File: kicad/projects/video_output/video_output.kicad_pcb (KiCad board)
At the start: 2 copper layers, 203.2 x 97.8 mm, 22 parts, among them J1 peripheral_addr_bus_connector, J2 peripheral_aux_connector, J3 peripheral_membank_connector, J4 Conn_01x16_Socket, J5 Conn_01x16_Socket, U1 628128_DIP32_SSOP32, U10 74HC157, U11 74HC157, U2 628128_DIP32_SSOP32, U3 74HC245, U4 74HC245, U5 74HC245, U6 74HC245, U7 74HC574, U8 74HC245, U9 74HC245

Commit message: Start roughing in video output.
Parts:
- added C2: 20pF, Capacitor_THT:C_Disc_D5.0mm_W2.5mm_P5.00mm, F.Cu at (-17.2, 30.1)
- added C3: 0pF, Capacitor_THT:C_Disc_D5.0mm_W2.5mm_P5.00mm, F.Cu at (-17.2, 34.1)
- added J6: Conn_01x02_Socket, Connector_PinSocket_2.54mm:PinSocket_1x02_P2.54mm_Horizontal, F.Cu at (61.0, 94.0)
- added J7: DE15_Receptacle_HighDensity, Connector_Dsub:DSUB-15_Female_Horizontal_P2.77x2.84mm_EdgePinOffset9.90mm_Housed_MountingHolesOffset11.32mm, F.Cu at (-67.9, 145.9)
- added R2: 4.7K, Resistor_THT:R_Axial_DIN0207_L6.3mm_D2.5mm_P10.16mm_Horizontal, F.Cu at (-30.5, 30.1)
- added R3: 4.7K, Resistor_THT:R_Axial_DIN0207_L6.3mm_D2.5mm_P10.16mm_Horizontal, F.Cu at (-30.5, 34.1)
- added R4: 10K, Resistor_THT:R_Axial_DIN0207_L6.3mm_D2.5mm_P10.16mm_Horizontal, F.Cu at (-30.5, 38.2)
- added R5: 10K, Resistor_THT:R_Axial_DIN0207_L6.3mm_D2.5mm_P10.16mm_Horizontal, F.Cu at (-30.5, 42.2)
- added R6: 10K, Resistor_THT:R_Axial_DIN0207_L6.3mm_D2.5mm_P10.16mm_Horizontal, F.Cu at (-30.5, 46.3)
- added R7: 10K, Resistor_THT:R_Axial_DIN0207_L6.3mm_D2.5mm_P10.16mm_Horizontal, F.Cu at (-30.5, 50.3)
- added R8: 10K, Resistor_THT:R_Axial_DIN0207_L6.3mm_D2.5mm_P10.16mm_Horizontal, F.Cu at (-30.5, 54.4)
- added R9: 10K, Resistor_THT:R_Axial_DIN0207_L6.3mm_D2.5mm_P10.16mm_Horizontal, F.Cu at (-30.5, 58.4)
- added U12: 74HC10, Package_DIP:DIP-14_W7.62mm_Socket, F.Cu at (106.7, 109.2)
- added U13: 74HC02, Package_DIP:DIP-14_W7.62mm_Socket, F.Cu at (106.7, 94.0)
- added U14: 74HC08, Package_DIP:DIP-14_W7.62mm_Socket, F.Cu at (132.1, 109.2)
- added U15: 74HC123, Package_DIP:DIP-16_W7.62mm_Socket, F.Cu at (104.1, 63.5)
- added U16: 74HC32, Package_DIP:DIP-14_W7.62mm_Socket, F.Cu at (132.1, 94.0)
- added U17: 74HC04, Package_DIP:DIP-14_W7.62mm_Socket, F.Cu at (106.7, 78.7)
- added U9: 74HC574, Package_DIP:DIP-20_W7.62mm_Socket, F.Cu at (73.7, 109.2)
- moved U6 196.8 mm to (68.6, -10.2)
- moved U3 114.3 mm to (226.1, 114.3)
- moved U9 107.2 mm to (177.8, 114.3)
- moved U2 64.3 mm to (210.8, 83.8)
- moved U5 43.4 mm to (226.1, 99.1)
- moved U1 39.4 mm to (162.6, 83.8)
- moved U10 37.5 mm to (132.1, 63.5)
- moved U4 34.1 mm to (177.8, 99.1)
- moved U11 18.0 mm to (132.1, 78.7)
- moved U8 17.0 mm to (58.4, 109.2), turned to 0 degrees
- moved U7 16.1 mm to (88.9, 109.2), turned to 0 degrees
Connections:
- J2 pad 10: /RFM -> /MEM_ACT
- J2 pad 12: /WTM -> /~{R}/W
- J4 pad 1: unconnected-(J4-Pin_1-Pad1) -> /COL_B_00
- J4 pad 10: unconnected-(J4-Pin_10-Pad10) -> /ROW_B_01
- J4 pad 11: unconnected-(J4-Pin_11-Pad11) -> /ROW_B_02
- J4 pad 12: unconnected-(J4-Pin_12-Pad12) -> /ROW_B_03
- J4 pad 13: unconnected-(J4-Pin_13-Pad13) -> /ROW_B_04
- J4 pad 14: unconnected-(J4-Pin_14-Pad14) -> /ROW_B_05
- J4 pad 15: unconnected-(J4-Pin_15-Pad15) -> /ROW_B_06
- J4 pad 2: unconnected-(J4-Pin_2-Pad2) -> /COL_B_01
- J4 pad 3: unconnected-(J4-Pin_3-Pad3) -> /COL_B_02
- J4 pad 4: unconnected-(J4-Pin_4-Pad4) -> /COL_B_03
- J4 pad 5: unconnected-(J4-Pin_5-Pad5) -> /COL_B_04
- J4 pad 6: unconnected-(J4-Pin_6-Pad6) -> /COL_B_05
- J4 pad 7: unconnected-(J4-Pin_7-Pad7) -> /COL_B_06
- J4 pad 8: unconnected-(J4-Pin_8-Pad8) -> /COL_B_07
- J4 pad 9: unconnected-(J4-Pin_9-Pad9) -> /ROW_B_00
- J5 pad 1: unconnected-(J5-Pin_1-Pad1) -> /COL_A_00
- J5 pad 10: unconnected-(J5-Pin_10-Pad10) -> /ROW_A_01
- J5 pad 11: unconnected-(J5-Pin_11-Pad11) -> /ROW_A_02
- J5 pad 12: unconnected-(J5-Pin_12-Pad12) -> /ROW_A_03
- J5 pad 13: unconnected-(J5-Pin_13-Pad13) -> /ROW_A_04
- J5 pad 14: unconnected-(J5-Pin_14-Pad14) -> /ROW_A_05
- J5 pad 15: unconnected-(J5-Pin_15-Pad15) -> /ROW_A_06
- J5 pad 2: unconnected-(J5-Pin_2-Pad2) -> /COL_A_01
- J5 pad 3: unconnected-(J5-Pin_3-Pad3) -> /COL_A_02
- J5 pad 4: unconnected-(J5-Pin_4-Pad4) -> /COL_A_03
- J5 pad 5: unconnected-(J5-Pin_5-Pad5) -> /COL_A_04
- J5 pad 6: unconnected-(J5-Pin_6-Pad6) -> /COL_A_05
- J5 pad 7: unconnected-(J5-Pin_7-Pad7) -> /COL_A_06
- J5 pad 8: unconnected-(J5-Pin_8-Pad8) -> /COL_A_07
- J5 pad 9: unconnected-(J5-Pin_9-Pad9) -> /ROW_A_00
- U1 pad 10: unconnected-(U1-A2-Pad10) -> /COL_B_02
- U1 pad 11: unconnected-(U1-A1-Pad11) -> /COL_B_01
- U1 pad 12: unconnected-(U1-A0-Pad12) -> /COL_B_00
- U1 pad 13: unconnected-(U1-Q0-Pad13) -> /PIX_R_B_00
- U1 pad 14: unconnected-(U1-Q1-Pad14) -> /PIX_R_B_01
- U1 pad 15: unconnected-(U1-Q2-Pad15) -> /PIX_G_B_00
- U1 pad 17: unconnected-(U1-Q3-Pad17) -> /PIX_G_B_01
- U1 pad 18: unconnected-(U1-Q4-Pad18) -> /PIX_B_B_00
- U1 pad 19: unconnected-(U1-Q5-Pad19) -> /PIX_B_B_01
- U1 pad 2: unconnected-(U1-A16-Pad2) -> GND
- U1 pad 20: unconnected-(U1-Q6-Pad20) -> Net-(U1-Q6)
- U1 pad 21: unconnected-(U1-Q7-Pad21) -> Net-(U1-Q7)
- U1 pad 23: unconnected-(U1-A10-Pad23) -> /ROW_B_02
- U1 pad 25: unconnected-(U1-A11-Pad25) -> /ROW_B_03
- U1 pad 26: unconnected-(U1-A9-Pad26) -> /ROW_B_01
- U1 pad 27: unconnected-(U1-A8-Pad27) -> /ROW_B_00
- U1 pad 28: unconnected-(U1-A13-Pad28) -> /ROW_B_05
- U1 pad 3: unconnected-(U1-A14-Pad3) -> /ROW_B_06
- U1 pad 31: unconnected-(U1-A15-Pad31) -> GND
- U1 pad 4: unconnected-(U1-A12-Pad4) -> /ROW_B_04
- U1 pad 5: unconnected-(U1-A7-Pad5) -> /COL_B_07
- U1 pad 6: unconnected-(U1-A6-Pad6) -> /COL_B_06
- U1 pad 7: unconnected-(U1-A5-Pad7) -> /COL_B_05
- U1 pad 8: unconnected-(U1-A4-Pad8) -> /COL_B_04
- U1 pad 9: unconnected-(U1-A3-Pad9) -> /COL_B_03
- U2 pad 10: unconnected-(U2-A2-Pad10) -> /COL_A_02
- U2 pad 11: unconnected-(U2-A1-Pad11) -> /COL_A_01
- U2 pad 12: unconnected-(U2-A0-Pad12) -> /COL_A_00
- U2 pad 13: unconnected-(U2-Q0-Pad13) -> /PIX_R_A_00
- U2 pad 14: unconnected-(U2-Q1-Pad14) -> /PIX_R_A_01
- U2 pad 15: unconnected-(U2-Q2-Pad15) -> /PIX_G_A_00
- U2 pad 17: unconnected-(U2-Q3-Pad17) -> /PIX_G_A_01
- U2 pad 18: unconnected-(U2-Q4-Pad18) -> /PIX_B_A_00
- U2 pad 19: unconnected-(U2-Q5-Pad19) -> /PIX_B_A_01
- U2 pad 2: unconnected-(U2-A16-Pad2) -> GND
- U2 pad 20: unconnected-(U2-Q6-Pad20) -> Net-(U2-Q6)
- U2 pad 21: unconnected-(U2-Q7-Pad21) -> Net-(U2-Q7)
- U2 pad 23: unconnected-(U2-A10-Pad23) -> /ROW_A_02
- U2 pad 25: unconnected-(U2-A11-Pad25) -> /ROW_A_03
- U2 pad 26: unconnected-(U2-A9-Pad26) -> /ROW_A_01
- U2 pad 27: unconnected-(U2-A8-Pad27) -> /ROW_A_00
- U2 pad 28: unconnected-(U2-A13-Pad28) -> /ROW_A_05
- U2 pad 3: unconnected-(U2-A14-Pad3) -> /ROW_A_06
- U2 pad 31: unconnected-(U2-A15-Pad31) -> GND
- U2 pad 4: unconnected-(U2-A12-Pad4) -> /ROW_A_04
- U2 pad 5: unconnected-(U2-A7-Pad5) -> /COL_A_07
- U2 pad 6: unconnected-(U2-A6-Pad6) -> /COL_A_06
- U2 pad 7: unconnected-(U2-A5-Pad7) -> /COL_A_05
- U2 pad 8: unconnected-(U2-A4-Pad8) -> /COL_A_04
- U2 pad 9: unconnected-(U2-A3-Pad9) -> /COL_A_03

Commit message: Bit of work on video output schematic.
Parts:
- added C4: C, Capacitor_THT:C_Disc_D5.0mm_W2.5mm_P5.00mm, F.Cu at (-35.6, 76.3)
- added C5: C, Capacitor_THT:C_Disc_D5.0mm_W2.5mm_P5.00mm, F.Cu at (-35.6, 80.3)
- added C6: C, Capacitor_THT:C_Disc_D5.0mm_W2.5mm_P5.00mm, F.Cu at (-35.6, 84.4)
- added C7: C, Capacitor_THT:C_Disc_D5.0mm_W2.5mm_P5.00mm, F.Cu at (-35.6, 88.4)
- added C8: C, Capacitor_THT:C_Disc_D5.0mm_W2.5mm_P5.00mm, F.Cu at (-35.6, 92.5)
- added C9: C, Capacitor_THT:C_Disc_D5.0mm_W2.5mm_P5.00mm, F.Cu at (-35.6, 96.5)
- added RN1: 10K, Resistor_THT:R_Array_SIP5, F.Cu at (248.9, 104.1)
- added RN2: 10K, Resistor_THT:R_Array_SIP5, F.Cu at (205.7, 104.1)
- added RN3: 10K, Resistor_THT:R_Array_SIP5, F.Cu at (248.9, 121.9)
- added RN4: 10K, Resistor_THT:R_Array_SIP5, F.Cu at (205.7, 121.9)
- moved U6 167.8 mm to (175.3, 119.4)
- moved U9 152.6 mm to (25.4, 121.9)
- moved U5 21.7 mm to (218.4, 119.4)
- moved U3 14.8 mm to (218.4, 101.6)
- moved U4 3.59 mm to (175.3, 101.6)
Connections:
- U1 pad 13: /PIX_R_B_00 -> /PIX_B_R_00
- U1 pad 14: /PIX_R_B_01 -> /PIX_B_R_01
- U1 pad 15: /PIX_G_B_00 -> /PIX_B_G_00
- U1 pad 16: unconnected-(U1-GND-Pad16) -> GND
- U1 pad 17: /PIX_G_B_01 -> /PIX_B_G_01
- U1 pad 22: unconnected-(U1-~{CS1}-Pad22) -> GND
- U1 pad 24: unconnected-(U1-~{OE}-Pad24) -> GND
- U1 pad 29: unconnected-(U1-~{WE}-Pad29) -> /B_RAM_~{WE}
- U1 pad 30: unconnected-(U1-CS2-Pad30) -> VCC
- U1 pad 32: unconnected-(U1-VCC-Pad32) -> VCC
- U10 pad 10: unconnected-(U10-3B-Pad10) -> VCC
- U10 pad 11: unconnected-(U10-3A-Pad11) -> /RAM_~{WE}
- U10 pad 15: unconnected-(U10-~{G}-Pad15) -> GND
- U10 pad 2: unconnected-(U10-1A-Pad2) -> /DATA_BUF_~{OE}
- U10 pad 3: unconnected-(U10-1B-Pad3) -> VCC
- U10 pad 4: unconnected-(U10-1Y-Pad4) -> /B_DATA_BUF_~{OE}
- U10 pad 5: unconnected-(U10-2A-Pad5) -> /DATA_BUF_DIR
- U10 pad 6: unconnected-(U10-2B-Pad6) -> GND
- U10 pad 7: unconnected-(U10-2Y-Pad7) -> /B_DATA_BUF_DIR
- U10 pad 9: unconnected-(U10-3Y-Pad9) -> /B_RAM_~{WE}
- U11 pad 10: unconnected-(U11-3B-Pad10) -> VCC
- U11 pad 11: unconnected-(U11-3A-Pad11) -> /RAM_~{WE}
- U11 pad 15: unconnected-(U11-~{G}-Pad15) -> GND
- U11 pad 2: unconnected-(U11-1A-Pad2) -> /DATA_BUF_~{OE}
- U11 pad 3: unconnected-(U11-1B-Pad3) -> VCC
- U11 pad 4: unconnected-(U11-1Y-Pad4) -> /A_DATA_BUF_~{OE}
- U11 pad 5: unconnected-(U11-2A-Pad5) -> /DATA_BUF_DIR
- U11 pad 6: unconnected-(U11-2B-Pad6) -> GND
- U11 pad 7: unconnected-(U11-2Y-Pad7) -> /A_DATA_BUF_DIR
- U11 pad 9: unconnected-(U11-3Y-Pad9) -> /A_RAM_~{WE}
- U14 pad 11: /DATA_BUF_DIR -> Net-(U14-Pad11)
- U16 pad 1: /DATA_BUF_DIR -> Net-(U14-Pad11)
- U2 pad 13: /PIX_R_A_00 -> /PIX_A_R_00
- U2 pad 14: /PIX_R_A_01 -> /PIX_A_R_01
- U2 pad 15: /PIX_G_A_00 -> /PIX_A_G_00
- U2 pad 16: unconnected-(U2-GND-Pad16) -> GND
- U2 pad 17: /PIX_G_A_01 -> /PIX_A_G_01
- U2 pad 18: /PIX_B_A_00 -> /PIX_A_B_00
- U2 pad 19: /PIX_B_A_01 -> /PIX_A_B_01
- U2 pad 22: unconnected-(U2-~{CS1}-Pad22) -> GND
- U2 pad 24: unconnected-(U2-~{OE}-Pad24) -> GND
- U2 pad 29: unconnected-(U2-~{WE}-Pad29) -> /A_RAM_~{WE}
- U2 pad 30: unconnected-(U2-CS2-Pad30) -> VCC
- U2 pad 32: unconnected-(U2-VCC-Pad32) -> VCC
- U3 pad 10: unconnected-(U3-GND-Pad10) -> GND
- U3 pad 11: unconnected-(U3-B8-Pad11) -> Net-(RN1-R3)
- U3 pad 12: unconnected-(U3-B7-Pad12) -> Net-(RN1-R4)
- U3 pad 13: unconnected-(U3-B6-Pad13) -> /PIX_A_R_00
- U3 pad 14: unconnected-(U3-B5-Pad14) -> /PIX_A_R_01
- U3 pad 15: unconnected-(U3-B4-Pad15) -> /PIX_A_G_00
- U3 pad 16: unconnected-(U3-B3-Pad16) -> /PIX_A_G_01
- U3 pad 17: unconnected-(U3-B2-Pad17) -> /PIX_A_B_00
- U3 pad 18: unconnected-(U3-B1-Pad18) -> /PIX_A_B_01
- U3 pad 2: unconnected-(U3-A1-Pad2) -> /PIX_B_01
- U3 pad 20: unconnected-(U3-VCC-Pad20) -> VCC
- U3 pad 3: unconnected-(U3-A2-Pad3) -> /PIX_B_00
- U3 pad 4: unconnected-(U3-A3-Pad4) -> /PIX_G_01
- U3 pad 5: unconnected-(U3-A3-Pad5) -> /PIX_G_00
- U3 pad 6: unconnected-(U3-A5-Pad6) -> /PIX_R_01
- U3 pad 7: unconnected-(U3-A6-Pad7) -> /PIX_R_00
- U3 pad 8: unconnected-(U3-A7-Pad8) -> Net-(RN1-R1)
- U3 pad 9: unconnected-(U3-A8-Pad9) -> Net-(RN1-R2)
- U4 pad 10: unconnected-(U4-GND-Pad10) -> GND
- U4 pad 11: unconnected-(U4-B8-Pad11) -> Net-(RN2-R3)
- U4 pad 12: unconnected-(U4-B7-Pad12) -> Net-(RN2-R4)
- U4 pad 13: unconnected-(U4-B6-Pad13) -> /PIX_B_R_00
- U4 pad 14: unconnected-(U4-B5-Pad14) -> /PIX_B_R_01
- U4 pad 15: unconnected-(U4-B4-Pad15) -> /PIX_B_G_00
- U4 pad 16: unconnected-(U4-B3-Pad16) -> /PIX_B_G_01
- U4 pad 17: unconnected-(U4-B2-Pad17) -> /PIX_B_B_00
- U4 pad 18: unconnected-(U4-B1-Pad18) -> /PIX_B_B_01
- U4 pad 2: unconnected-(U4-A1-Pad2) -> /PIX_B_01
- U4 pad 20: unconnected-(U4-VCC-Pad20) -> VCC
- U4 pad 3: unconnected-(U4-A2-Pad3) -> /PIX_B_00
- U4 pad 4: unconnected-(U4-A3-Pad4) -> /PIX_G_01
- U4 pad 5: unconnected-(U4-A3-Pad5) -> /PIX_G_00
- U4 pad 6: unconnected-(U4-A5-Pad6) -> /PIX_R_01
- U4 pad 7: unconnected-(U4-A6-Pad7) -> /PIX_R_00
- U4 pad 8: unconnected-(U4-A7-Pad8) -> Net-(RN2-R1)
- U4 pad 9: unconnected-(U4-A8-Pad9) -> Net-(RN2-R2)
- U5 pad 10: unconnected-(U5-GND-Pad10) -> GND
- U5 pad 11: unconnected-(U5-B8-Pad11) -> Net-(RN3-R3)
- U5 pad 12: unconnected-(U5-B7-Pad12) -> Net-(RN3-R4)
- U5 pad 13: unconnected-(U5-B6-Pad13) -> /PIX_A_R_00
- U5 pad 14: unconnected-(U5-B5-Pad14) -> /PIX_A_R_01
- U5 pad 15: unconnected-(U5-B4-Pad15) -> /PIX_A_G_00
- U5 pad 16: unconnected-(U5-B3-Pad16) -> /PIX_A_G_01
- U5 pad 17: unconnected-(U5-B2-Pad17) -> /PIX_A_B_00
- U5 pad 18: unconnected-(U5-B1-Pad18) -> /PIX_A_B_01
- U5 pad 2: unconnected-(U5-A1-Pad2) -> /DATA_BUS_05
- U5 pad 20: unconnected-(U5-VCC-Pad20) -> VCC
- U5 pad 3: unconnected-(U5-A2-Pad3) -> /DATA_BUS_04
- U5 pad 4: unconnected-(U5-A3-Pad4) -> /DATA_BUS_03
- U5 pad 5: unconnected-(U5-A3-Pad5) -> /DATA_BUS_02
- U5 pad 6: unconnected-(U5-A5-Pad6) -> /DATA_BUS_01
- U5 pad 7: unconnected-(U5-A6-Pad7) -> /DATA_BUS_00
- U5 pad 8: unconnected-(U5-A7-Pad8) -> Net-(RN3-R1)
- U5 pad 9: unconnected-(U5-A8-Pad9) -> Net-(RN3-R2)
- U6 pad 10: unconnected-(U6-GND-Pad10) -> GND
- U6 pad 11: unconnected-(U6-B8-Pad11) -> Net-(RN4-R3)
- U6 pad 12: unconnected-(U6-B7-Pad12) -> Net-(RN4-R4)
- U6 pad 13: unconnected-(U6-B6-Pad13) -> /PIX_B_R_00
- U6 pad 14: unconnected-(U6-B5-Pad14) -> /PIX_B_R_01
- U6 pad 15: unconnected-(U6-B4-Pad15) -> /PIX_B_G_00
- U6 pad 16: unconnected-(U6-B3-Pad16) -> /PIX_B_G_01
- U6 pad 17: unconnected-(U6-B2-Pad17) -> /PIX_B_B_00
- U6 pad 18: unconnected-(U6-B1-Pad18) -> /PIX_B_B_01
- U6 pad 2: unconnected-(U6-A1-Pad2) -> /DATA_BUS_05
- U6 pad 20: unconnected-(U6-VCC-Pad20) -> VCC
- U6 pad 3: unconnected-(U6-A2-Pad3) -> /DATA_BUS_04
- U6 pad 4: unconnected-(U6-A3-Pad4) -> /DATA_BUS_03
- U6 pad 5: unconnected-(U6-A3-Pad5) -> /DATA_BUS_02
- U6 pad 6: unconnected-(U6-A5-Pad6) -> /DATA_BUS_01
- U6 pad 7: unconnected-(U6-A6-Pad7) -> /DATA_BUS_00
- U6 pad 8: unconnected-(U6-A7-Pad8) -> Net-(RN4-R1)
- U6 pad 9: unconnected-(U6-A8-Pad9) -> Net-(RN4-R2)
- U7 pad 1: unconnected-(U7-OE-Pad1) -> GND
- U7 pad 18: unconnected-(U7-Q1-Pad18) -> /VSYNC_CLOCKED
- U7 pad 19: unconnected-(U7-Q0-Pad19) -> /HSYNC_CLOCKED
- U7 pad 2: unconnected-(U7-D0-Pad2) -> /HSYNC
- U7 pad 3: unconnected-(U7-D1-Pad3) -> /VSYNC
- U7 pad 4: unconnected-(U7-D2-Pad4) -> GND
- U7 pad 5: unconnected-(U7-D3-Pad5) -> GND
- U7 pad 6: unconnected-(U7-D4-Pad6) -> GND
- U7 pad 7: unconnected-(U7-D5-Pad7) -> GND
- U7 pad 8: unconnected-(U7-D6-Pad8) -> GND
- U7 pad 9: unconnected-(U7-D7-Pad9) -> GND
- U8 pad 2: unconnected-(U8-A1-Pad2) -> /PIX_R_00_CLOCKED
- U8 pad 3: unconnected-(U8-A2-Pad3) -> /PIX_R_01_CLOCKED
- U8 pad 4: unconnected-(U8-A3-Pad4) -> /PIX_G_00_CLOCKED
- U8 pad 5: unconnected-(U8-A3-Pad5) -> /PIX_G_01_CLOCKED
- U8 pad 6: unconnected-(U8-A5-Pad6) -> /PIX_B_00_CLOCKED
- U8 pad 7: unconnected-(U8-A6-Pad7) -> /PIX_B_01_CLOCKED
- U8 pad 8: unconnected-(U8-A7-Pad8) -> /HSYNC_CLOCKED
- U8 pad 9: unconnected-(U8-A8-Pad9) -> /VSYNC_CLOCKED
- U9 pad 14: unconnected-(U9-Q5-Pad14) -> /PIX_B_01_CLOCKED
- U9 pad 15: unconnected-(U9-Q4-Pad15) -> /PIX_B_00_CLOCKED
- U9 pad 16: unconnected-(U9-Q3-Pad16) -> /PIX_G_01_CLOCKED
- U9 pad 17: unconnected-(U9-Q2-Pad17) -> /PIX_G_00_CLOCKED
- U9 pad 18: unconnected-(U9-Q1-Pad18) -> /PIX_R_01_CLOCKED
- U9 pad 19: unconnected-(U9-Q0-Pad19) -> /PIX_R_00_CLOCKED
- U9 pad 2: unconnected-(U9-D0-Pad2) -> /PIX_R_00
- U9 pad 3: unconnected-(U9-D1-Pad3) -> /PIX_R_01
- U9 pad 4: unconnected-(U9-D2-Pad4) -> /PIX_G_00
- U9 pad 5: unconnected-(U9-D3-Pad5) -> /PIX_G_01
- U9 pad 6: unconnected-(U9-D4-Pad6) -> /PIX_B_00
- U9 pad 7: unconnected-(U9-D5-Pad7) -> /PIX_B_01
- U9 pad 8: unconnected-(U9-D6-Pad8) -> GND
- U9 pad 9: unconnected-(U9-D7-Pad9) -> GND

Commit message: Add music planning and some extra work planning video card layouts.
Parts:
- removed the U9 at (25.4, 121.9)
- added C10: C, Capacitor_THT:C_Disc_D5.0mm_W2.5mm_P5.00mm, F.Cu at (-45.6, 42.2)
- added C11: C, Capacitor_THT:C_Disc_D5.0mm_W2.5mm_P5.00mm, F.Cu at (-45.6, 46.3)
- added C12: C, Capacitor_THT:C_Disc_D5.0mm_W2.5mm_P5.00mm, F.Cu at (-45.6, 50.3)
- added C13: C, Capacitor_THT:C_Disc_D5.0mm_W2.5mm_P5.00mm, F.Cu at (-45.6, 54.4)
- added C14: C, Capacitor_THT:C_Disc_D5.0mm_W2.5mm_P5.00mm, F.Cu at (-45.6, 58.4)
- moved U14 39.7 mm to (106.7, 78.7)
- moved U17 39.7 mm to (132.1, 109.2)
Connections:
- U10 pad 16: unconnected-(U10-VCC-Pad16) -> VCC
- U10 pad 8: unconnected-(U10-GND-Pad8) -> GND
- U11 pad 16: unconnected-(U11-VCC-Pad16) -> VCC
- U11 pad 8: unconnected-(U11-GND-Pad8) -> GND
- U7 pad 10: unconnected-(U7-GND-Pad10) -> GND
- U7 pad 11: unconnected-(U7-Cp-Pad11) -> /PIXEL_CLK
- U7 pad 17: unconnected-(U7-Q2-Pad17) -> /ANYBLANK_CLOCKED
- U7 pad 20: unconnected-(U7-VCC-Pad20) -> VCC
- U7 pad 4: GND -> /ANYBLANK
- U8 pad 10: unconnected-(U8-GND-Pad10) -> GND
- U8 pad 20: unconnected-(U8-VCC-Pad20) -> VCC
- U9 pad 10: unconnected-(U9-GND-Pad10) -> GND
- U9 pad 11: unconnected-(U9-Cp-Pad11) -> /PIXEL_CLK
- U9 pad 20: unconnected-(U9-VCC-Pad20) -> VCC

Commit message: Bit more tweaking and fleshing out of video circuits.
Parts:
- added R10: 1.5K, Resistor_THT:R_Axial_DIN0207_L6.3mm_D2.5mm_P10.16mm_Horizontal, F.Cu at (68.7, 104.1)
- added R11: 680, Resistor_THT:R_Axial_DIN0207_L6.3mm_D2.5mm_P10.16mm_Horizontal, F.Cu at (72.7, 104.1)
- added R12: 1.5K, Resistor_THT:R_Axial_DIN0207_L6.3mm_D2.5mm_P10.16mm_Horizontal, F.Cu at (76.8, 104.1)
- added R13: 680, Resistor_THT:R_Axial_DIN0207_L6.3mm_D2.5mm_P10.16mm_Horizontal, F.Cu at (80.8, 104.1)
- added R14: 1.5K, Resistor_THT:R_Axial_DIN0207_L6.3mm_D2.5mm_P10.16mm_Horizontal, F.Cu at (84.8, 104.1)
- added R15: 680, Resistor_THT:R_Axial_DIN0207_L6.3mm_D2.5mm_P10.16mm_Horizontal, F.Cu at (88.9, 104.1)
- added RN5: 10K, Resistor_THT:R_Array_SIP9, F.Cu at (53.3, 132.1)
- moved R5 273.3 mm to (238.8, 88.9)
- moved R6 260.1 mm to (226.1, 88.9)
- moved R7 224.3 mm to (190.5, 88.9)
- moved R8 211.1 mm to (177.8, 88.9)
- moved R4 160.1 mm to (129.5, 43.2)
- moved R2 148.1 mm to (116.8, 45.7), turned to 180 degrees
- moved R3 137.3 mm to (106.7, 40.6)
- moved C3 123.9 mm to (106.7, 35.6)
- moved C2 123.9 mm to (106.7, 30.1)
- moved R9 96.4 mm to (61.0, 88.9)
- moved U16 15.2 mm to (132.1, 109.2)
- moved U17 15.2 mm to (132.1, 94.0)
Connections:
- U10 pad 1: unconnected-(U10-~{A}/B-Pad1) -> /~{BANK_SEL}
- U10 pad 13: unconnected-(U10-4B-Pad13) -> GND
- U10 pad 14: unconnected-(U10-4A-Pad14) -> GND
- U11 pad 1: unconnected-(U11-~{A}/B-Pad1) -> /BANK_SEL
- U11 pad 13: unconnected-(U11-4B-Pad13) -> GND
- U11 pad 14: unconnected-(U11-4A-Pad14) -> GND
- U16 pad 11: unconnected-(U16-Pad11) -> /ANYBLANK
- U16 pad 12: unconnected-(U16-Pad12) -> /HBLANK_CLOCKED
- U16 pad 13: unconnected-(U16-Pad13) -> /VBLANK_CLOCKED
- U17 pad 5: unconnected-(U17-Pad5) -> /BANK_SEL
- U17 pad 6: unconnected-(U17-Pad6) -> /~{BANK_SEL}
- U3 pad 1: unconnected-(U3-DIR-Pad1) -> GND
- U3 pad 19: unconnected-(U3-~{OE}-Pad19) -> /~{BANK_SEL}
- U4 pad 1: unconnected-(U4-DIR-Pad1) -> GND
- U4 pad 19: unconnected-(U4-~{OE}-Pad19) -> /BANK_SEL
- U5 pad 1: unconnected-(U5-DIR-Pad1) -> /A_DATA_BUF_DIR
- U5 pad 19: unconnected-(U5-~{OE}-Pad19) -> /A_DATA_BUF_~{OE}
- U6 pad 1: unconnected-(U6-DIR-Pad1) -> /B_DATA_BUF_DIR
- U6 pad 19: unconnected-(U6-~{OE}-Pad19) -> /B_DATA_BUF_~{OE}
- U7 pad 16: unconnected-(U7-Q3-Pad16) -> /VBLANK_CLOCKED
- U7 pad 17: /ANYBLANK_CLOCKED -> /HBLANK_CLOCKED
- U7 pad 4: /ANYBLANK -> /HBLANK
- U7 pad 5: GND -> /VBLANK
- U8 pad 1: unconnected-(U8-DIR-Pad1) -> VCC
- U8 pad 11: unconnected-(U8-B8-Pad11) -> /VSYNC_OUT
- U8 pad 12: unconnected-(U8-B7-Pad12) -> /HSYNC_OUT
- U8 pad 13: unconnected-(U8-B6-Pad13) -> /PIX_B_01_OUT
- U8 pad 14: unconnected-(U8-B5-Pad14) -> /PIX_B_00_OUT
- U8 pad 15: unconnected-(U8-B4-Pad15) -> /PIX_G_01_OUT
- U8 pad 16: unconnected-(U8-B3-Pad16) -> /PIX_G_00_OUT
- U8 pad 17: unconnected-(U8-B2-Pad17) -> /PIX_R_01_OUT
- U8 pad 18: unconnected-(U8-B1-Pad18) -> /PIX_R_00_OUT
- U8 pad 19: unconnected-(U8-~{OE}-Pad19) -> GND
- U9 pad 1: unconnected-(U9-OE-Pad1) -> /ANYBLANK

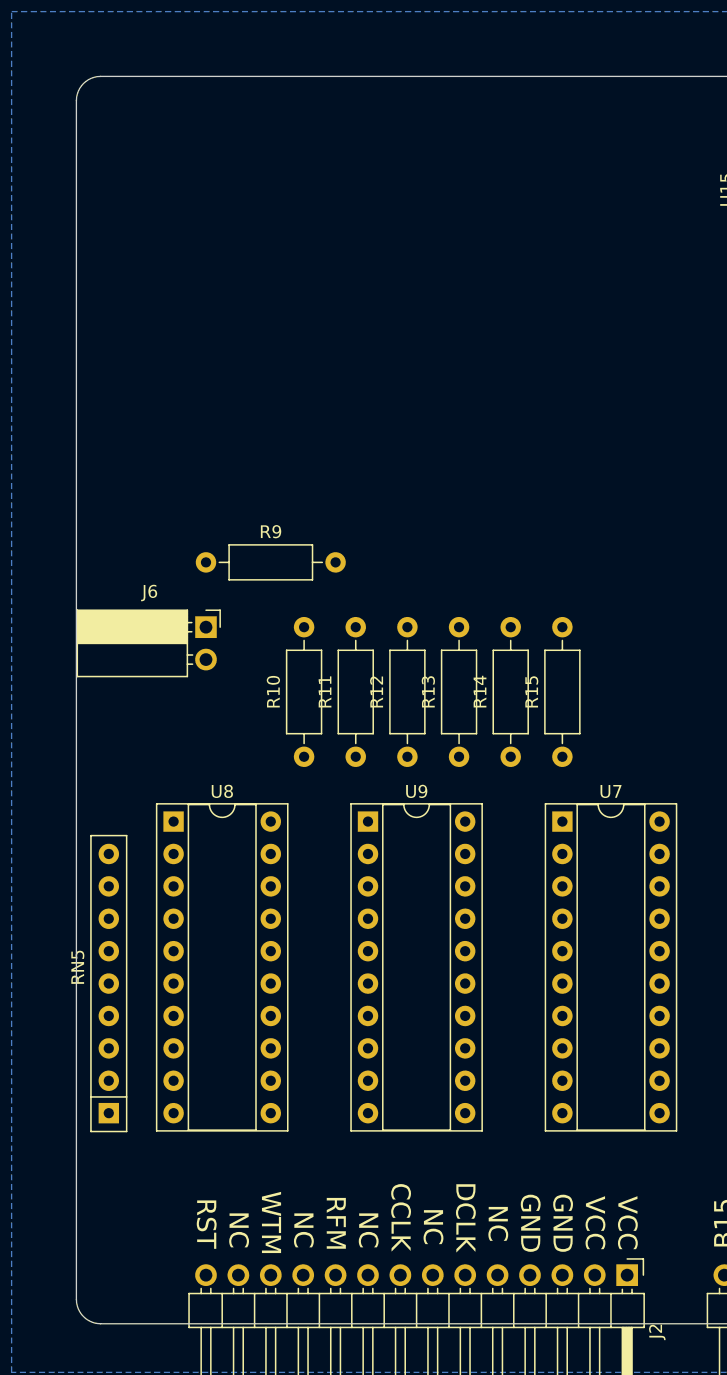
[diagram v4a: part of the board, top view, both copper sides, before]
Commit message: Adding video aux and some bits and bieces on video boards.
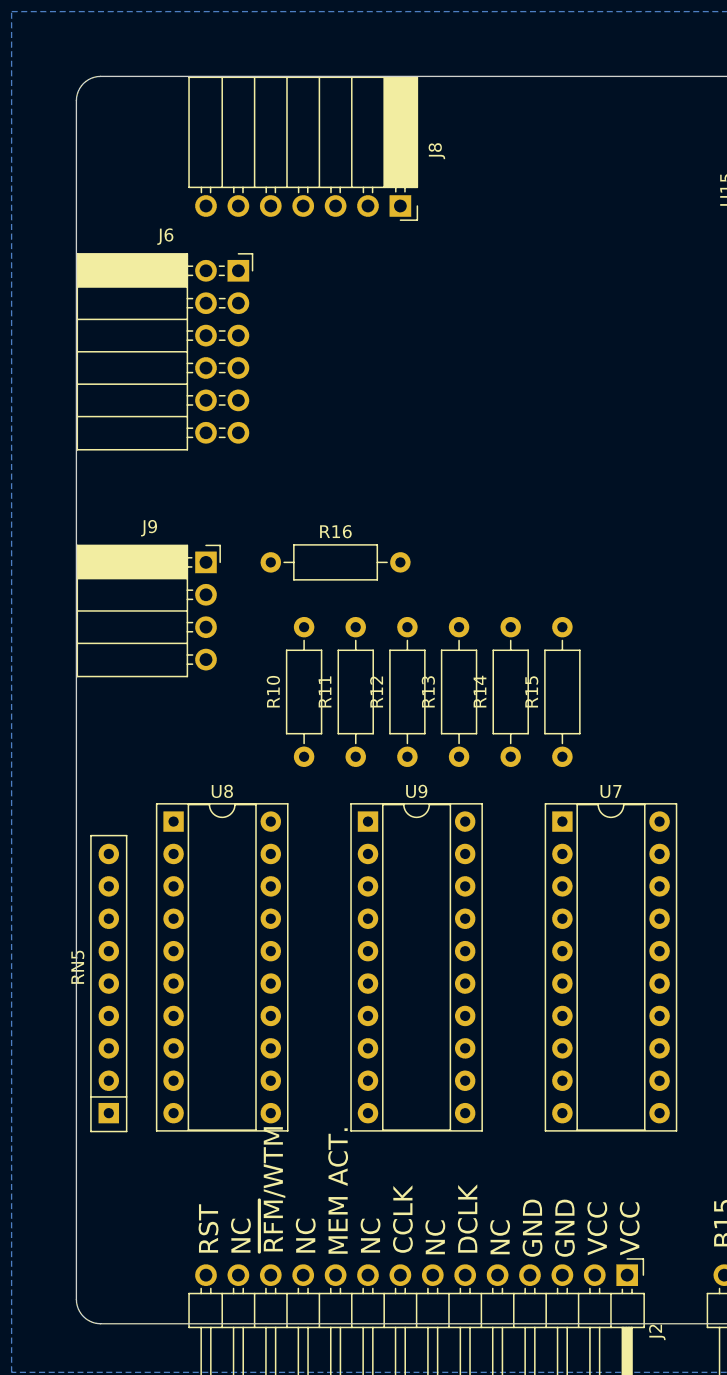
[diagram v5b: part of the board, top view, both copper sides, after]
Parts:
- removed R9: 10K, Resistor_THT:R_Axial_DIN0207_L6.3mm_D2.5mm_P10.16mm_Horizontal
- added J8: video_aux, Connector_PinSocket_2.54mm:PinSocket_1x07_P2.54mm_Horizontal, F.Cu at (76.2, 61.0)
- added J9: Conn_01x04_Socket, Connector_PinSocket_2.54mm:PinSocket_1x04_P2.54mm_Horizontal, F.Cu at (61.0, 88.9)
- added R16: 10K, Resistor_THT:R_Axial_DIN0207_L6.3mm_D2.5mm_P10.16mm_Horizontal, F.Cu at (66.0, 88.9)
- J6: value Conn_01x02_Socket -> Conn_02x06_Odd_Even; footprint Connector_PinSocket_2.54mm:PinSocket_1x02_P2.54mm_Horizontal -> Connector_PinSocket_2.54mm:PinSocket_2x06_P2.54mm_Horizontal
- moved J6 28.1 mm to (63.5, 66.0)
- turned J2 to 0 degrees
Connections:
- net /PIXEL_CLK renamed /PIXEL_CLK_MOD
- J6 pad 1: /ADDRESSED -> /PIX_R_OUT
- J6 pad 2: /ADDRESSED -> /PIX_R_OUT
